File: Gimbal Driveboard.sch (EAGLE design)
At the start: 23 parts, among them J2 APP_2POS_CONFIG12V_HORIZ, U1 OKI-78SR-5/1.5-W36HC, U2 MAX232D, U3 MAX232D

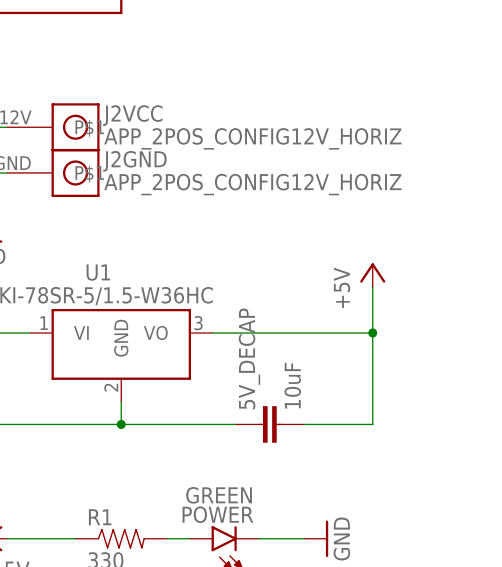
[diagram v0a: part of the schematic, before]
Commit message: Remade schematic to avoid physical interference with ethernet port
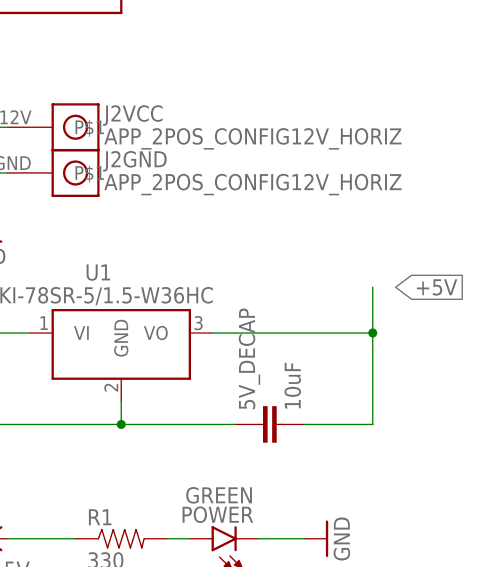
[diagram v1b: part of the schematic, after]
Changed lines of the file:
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@@
 <part name="GND7" library="supply1" deviceset="GND" device=""/>
 <part name="GND8" library="supply1" deviceset="GND" device=""/>
-<part name="P+14" library="supply1" deviceset="+5V" device=""/>
 <part name="GND20" library="supply1" deviceset="GND" device=""/>
 <part name="U1" library="MRDT-ICs" deviceset="OKI-78SR-*/1.5-W36?C" device="H" technology="5"/>
@@
 <instance part="GND7" gate="1" x="43.18" y="-5.08"/>
 <instance part="GND8" gate="1" x="91.44" y="-25.4"/>
-<instance part="P+14" gate="1" x="256.54" y="-43.18"/>
 <instance part="GND20" gate="1" x="213.36" y="-40.64"/>
 <instance part="U1" gate="G$1" x="226.06" y="-50.8"/>
@@
 </segment>
 <segment>
-<pinref part="P+14" gate="1" pin="+5V"/>
+<pinref part="R1" gate="G$1" pin="1"/>
+<pinref part="P+6" gate="1" pin="+5V"/>
+<wire x1="215.9" y1="-73.66" x2="223.52" y2="-73.66" width="0.1524" layer="91"/>
+</segment>
+<segment>
 <pinref part="5V_DECAP" gate="G$1" pin="2"/>
 <wire x1="248.92" y1="-60.96" x2="256.54" y2="-60.96" width="0.1524" layer="91"/>
@@
 <wire x1="238.76" y1="-50.8" x2="256.54" y2="-50.8" width="0.1524" layer="91"/>
 <junction x="256.54" y="-50.8"/>
-</segment>
-<segment>
-<pinref part="R1" gate="G$1" pin="1"/>
-<pinref part="P+6" gate="1" pin="+5V"/>
-<wire x1="215.9" y1="-73.66" x2="223.52" y2="-73.66" width="0.1524" layer="91"/>
+<label x="259.08" y="-45.72" size="1.778" layer="95" xref="yes"/>
 </segment>
 </net>

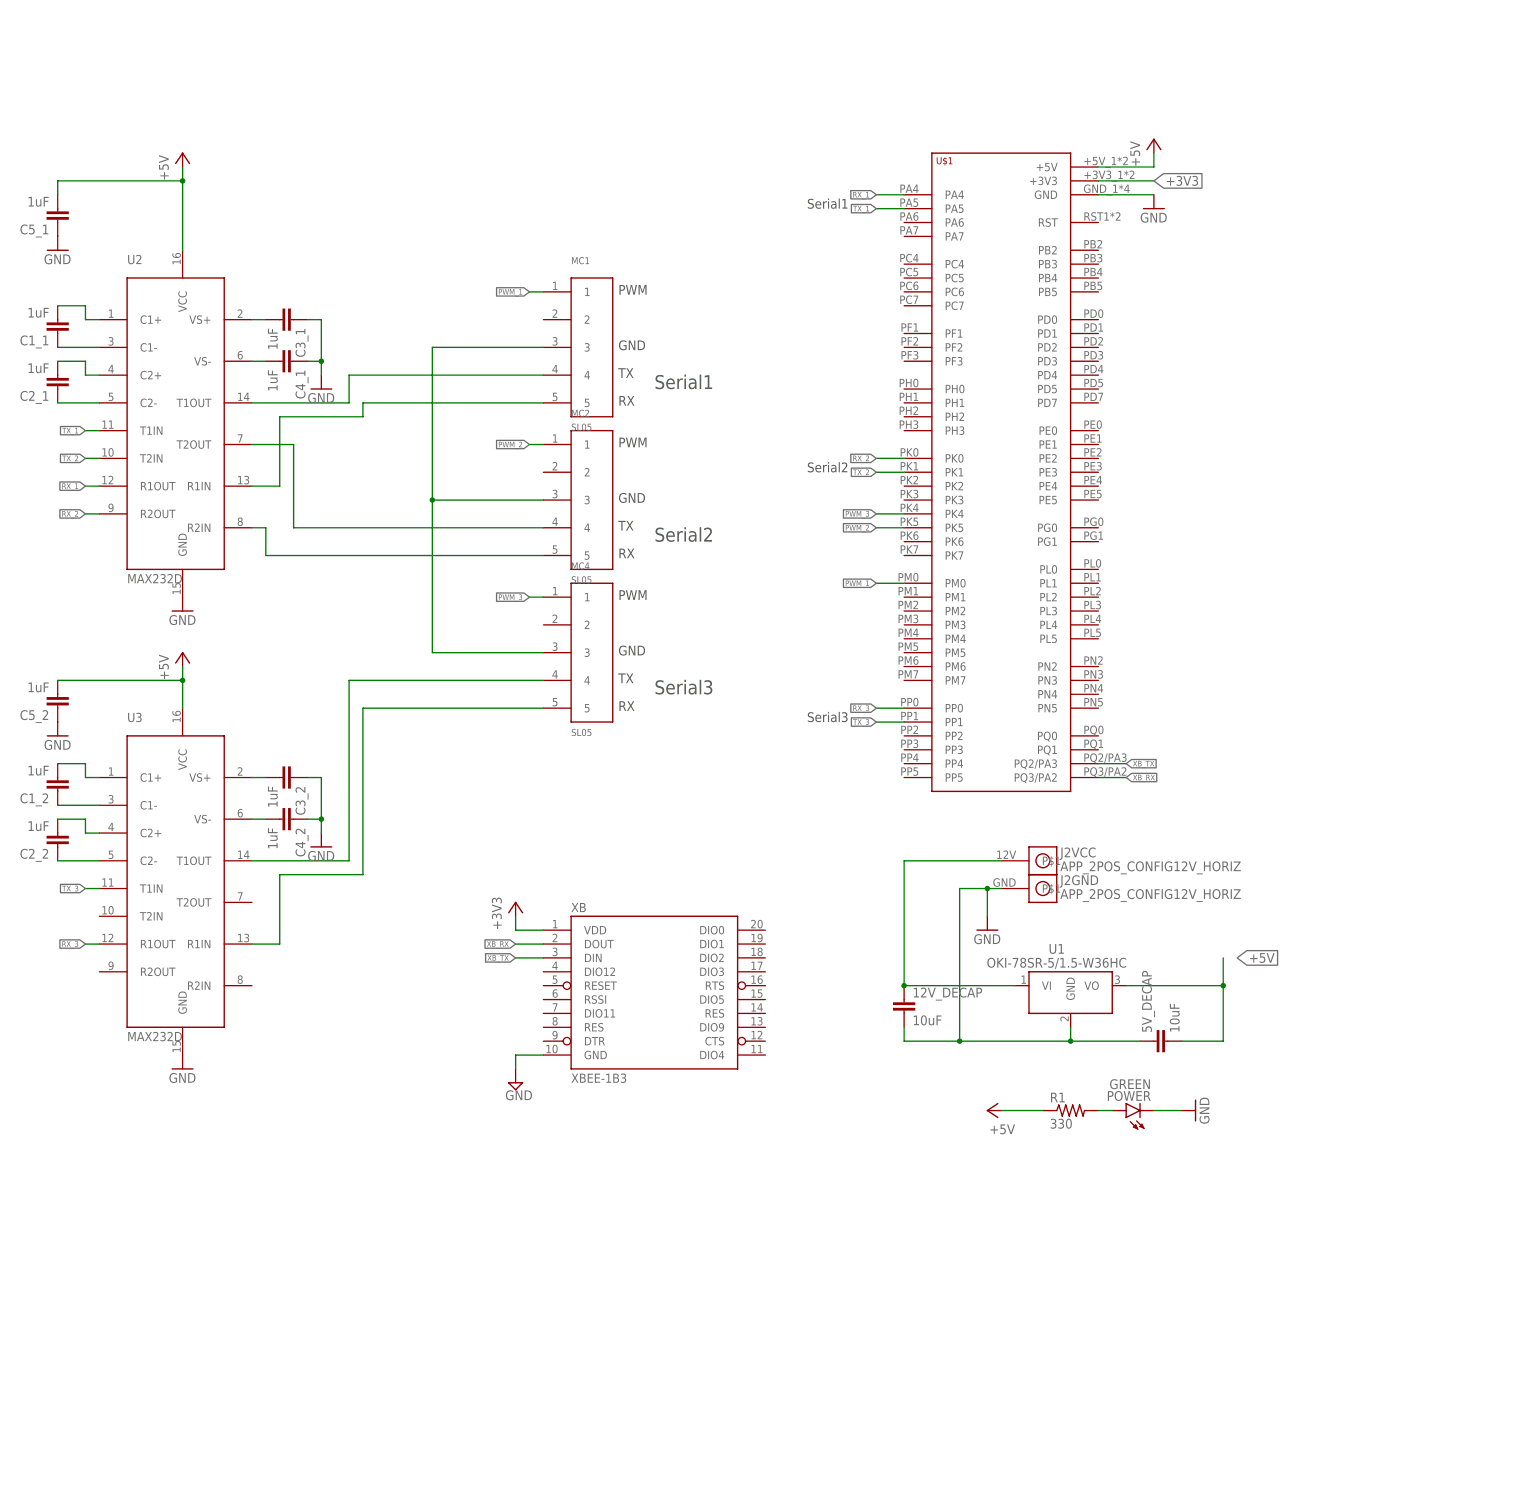
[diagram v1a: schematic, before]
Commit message: Updated schematic and board for final board review
added I2C Molex SL4
Added mounting tab and holes
cleaned up lines and traces
Added signature and board information
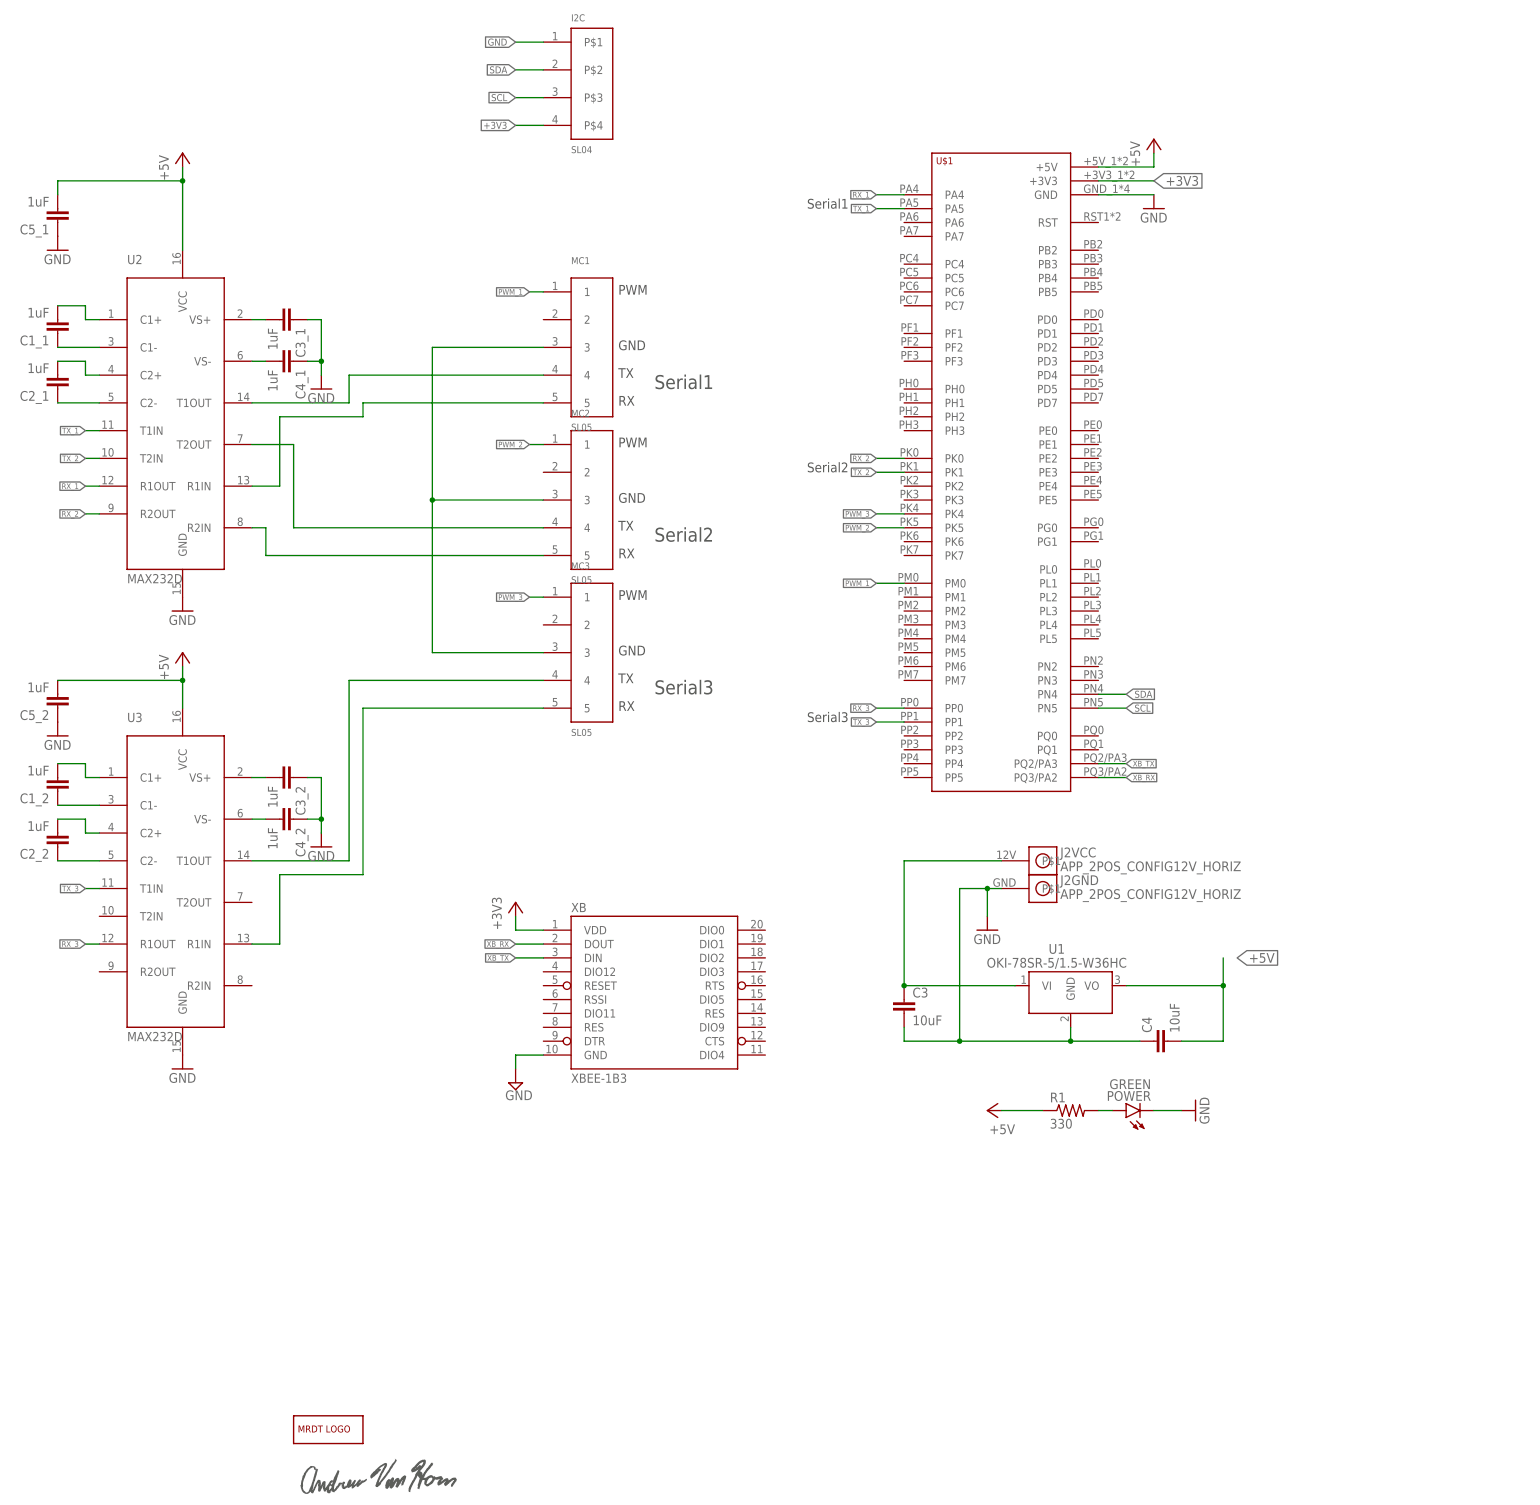
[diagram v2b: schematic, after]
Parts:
- added I2C: SL04, MRDT-Connectors:SL04
- added LOGO1: MRDT_LOGO, MRDT-Hardware:MRDT_LOGO
- added U$3: ANDREW_VAN_HORN_SIGNATURE, MRDT-Signatures:ANDREW_VAN_HORN_SIGNATURE
- renumbered 12V_DECAP to C3, 5V_DECAP to C4, MC4 to MC3
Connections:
- new net SCL: I2C.P$3, U$1.PN5
- new net SDA: I2C.P$2, U$1.PN4
- net +3V3: now also I2C.P$4
- net GND: now also I2C.P$1
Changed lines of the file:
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@@
 </variantdefs>
 <classes>
-<class number="0" name="default" width="0" drill="0">
+<class number="0" name="default" width="0.254" drill="0">
+<clearance class="0" value="0.254"/>
 </class>
 </classes>
@@
 <part name="MC1" library="MRDT-Connectors" deviceset="SL05" device="" value="SL05"/>
 <part name="MC2" library="MRDT-Connectors" deviceset="SL05" device="" value="SL05"/>
-<part name="MC4" library="MRDT-Connectors" deviceset="SL05" device="" value="SL05"/>
+<part name="MC3" library="MRDT-Connectors" deviceset="SL05" device="" value="SL05"/>
 <part name="P+3" library="supply1" deviceset="+5V" device=""/>
 <part name="GND3" library="supply1" deviceset="GND" device=""/>
@@
 <part name="U1" library="MRDT-ICs" deviceset="OKI-78SR-*/1.5-W36?C" device="H" technology="5"/>
 <part name="J2" library="MRDT-Connectors" deviceset="APP_2POS_CONFIG" device="12V_HORIZ"/>
-<part name="5V_DECAP" library="SparkFun-Capacitors" deviceset="CAP" device="0805" value="10uF"/>
-<part name="12V_DECAP" library="SparkFun-Capacitors" deviceset="CAP" device="0805" value="10uF"/>
+<part name="C4" library="SparkFun-Capacitors" deviceset="CAP" device="0805" value="10uF"/>
+<part name="C3" library="SparkFun-Capacitors" deviceset="CAP" device="0805" value="10uF"/>
 <part name="P+6" library="supply1" deviceset="+5V" device=""/>
 <part name="POWER" library="SparkFun-LED" deviceset="LED-GREEN" device="1206" value="GREEN"/>
@@
 <part name="+3V5" library="supply1" deviceset="+3V3" device=""/>
 <part name="SUPPLY6" library="supply2" deviceset="GND" device=""/>
+<part name="I2C" library="MRDT-Connectors" deviceset="SL04" device=""/>
+<part name="LOGO1" library="MRDT-Hardware" deviceset="MRDT_LOGO" device=""/>
+<part name="U$3" library="MRDT-Signatures" deviceset="ANDREW_VAN_HORN_SIGNATURE" device=""/>
 </parts>
 <sheets>
@@
 <instance part="MC1" gate="G$1" x="139.7" y="63.5"/>
 <instance part="MC2" gate="G$1" x="139.7" y="35.56"/>
-<instance part="MC4" gate="G$1" x="139.7" y="7.62"/>
+<instance part="MC3" gate="G$1" x="139.7" y="7.62"/>
 <instance part="P+3" gate="1" x="66.04" y="101.6"/>
 <instance part="GND3" gate="1" x="66.04" y="-66.04"/>
@@
 <instance part="J2" gate="GND" x="223.52" y="-33.02"/>
 <instance part="J2" gate="VCC" x="223.52" y="-27.94"/>
-<instance part="5V_DECAP" gate="G$1" x="246.38" y="-60.96" rot="R90"/>
-<instance part="12V_DECAP" gate="G$1" x="198.12" y="-55.88"/>
+<instance part="C4" gate="G$1" x="246.38" y="-60.96" rot="R90"/>
+<instance part="C3" gate="G$1" x="198.12" y="-55.88"/>
 <instance part="P+6" gate="1" x="213.36" y="-73.66" rot="R90"/>
 <instance part="POWER" gate="G$1" x="238.76" y="-73.66" rot="R90"/>
@@
 <instance part="+3V5" gate="G$1" x="127" y="-35.56"/>
 <instance part="SUPPLY6" gate="GND" x="127" y="-68.58"/>
+<instance part="I2C" gate="G$1" x="139.7" y="114.3"/>
+<instance part="LOGO1" gate="G$1" x="86.36" y="-134.62"/>
+<instance part="U$3" gate="G$1" x="86.36" y="-144.78"/>
 </instances>
 <busses>
@@
 <pinref part="MC2" gate="G$1" pin="3"/>
 <wire x1="132.08" y1="38.1" x2="111.76" y2="38.1" width="0.1524" layer="91"/>
-<pinref part="MC4" gate="G$1" pin="3"/>
+<pinref part="MC3" gate="G$1" pin="3"/>
 <wire x1="111.76" y1="38.1" x2="111.76" y2="10.16" width="0.1524" layer="91"/>
 <wire x1="111.76" y1="10.16" x2="132.08" y2="10.16" width="0.1524" layer="91"/>
@@
 <junction x="213.36" y="-33.02"/>
 <pinref part="J2" gate="GND" pin="P$1"/>
-<pinref part="12V_DECAP" gate="G$1" pin="2"/>
+<pinref part="C3" gate="G$1" pin="2"/>
 <wire x1="198.12" y1="-58.42" x2="198.12" y2="-60.96" width="0.1524" layer="91"/>
 <wire x1="198.12" y1="-60.96" x2="208.28" y2="-60.96" width="0.1524" layer="91"/>
 <junction x="208.28" y="-60.96"/>
-<pinref part="5V_DECAP" gate="G$1" pin="1"/>
+<pinref part="C4" gate="G$1" pin="1"/>
 <wire x1="241.3" y1="-60.96" x2="228.6" y2="-60.96" width="0.1524" layer="91"/>
 <junction x="228.6" y="-60.96"/>
@@
 <wire x1="127" y1="-63.5" x2="127" y2="-66.04" width="0.1524" layer="91"/>
 <pinref part="SUPPLY6" gate="GND" pin="GND"/>
+</segment>
+<segment>
+<pinref part="I2C" gate="G$1" pin="P$1"/>
+<wire x1="132.08" y1="121.92" x2="127" y2="121.92" width="0.1524" layer="91"/>
+<label x="127" y="121.92" size="1.27" layer="95" rot="R180" xref="yes"/>
 </segment>
 </net>
@@
 </segment>
 <segment>
-<pinref part="5V_DECAP" gate="G$1" pin="2"/>
+<pinref part="C4" gate="G$1" pin="2"/>
 <wire x1="248.92" y1="-60.96" x2="256.54" y2="-60.96" width="0.1524" layer="91"/>
 <wire x1="256.54" y1="-60.96" x2="256.54" y2="-50.8" width="0.1524" layer="91"/>
@@
 </segment>
 <segment>
-<pinref part="MC4" gate="G$1" pin="1"/>
+<pinref part="MC3" gate="G$1" pin="1"/>
 <wire x1="132.08" y1="20.32" x2="129.54" y2="20.32" width="0.1524" layer="91"/>
 <label x="129.54" y="20.32" size="1.016" layer="95" rot="R180" xref="yes"/>
@@
 <pinref part="U3" gate="G$1" pin="T1OUT"/>
 <wire x1="78.74" y1="-27.94" x2="96.52" y2="-27.94" width="0.1524" layer="91"/>
-<pinref part="MC4" gate="G$1" pin="4"/>
+<pinref part="MC3" gate="G$1" pin="4"/>
 <wire x1="96.52" y1="-27.94" x2="96.52" y2="5.08" width="0.1524" layer="91"/>
 <wire x1="96.52" y1="5.08" x2="132.08" y2="5.08" width="0.1524" layer="91"/>
@@
 <wire x1="83.82" y1="-43.18" x2="83.82" y2="-30.48" width="0.1524" layer="91"/>
 <wire x1="83.82" y1="-30.48" x2="99.06" y2="-30.48" width="0.1524" layer="91"/>
-<pinref part="MC4" gate="G$1" pin="5"/>
+<pinref part="MC3" gate="G$1" pin="5"/>
 <wire x1="132.08" y1="0" x2="99.06" y2="0" width="0.1524" layer="91"/>
 <wire x1="99.06" y1="0" x2="99.06" y2="-30.48" width="0.1524" layer="91"/>
@@
 <wire x1="198.12" y1="-27.94" x2="198.12" y2="-50.8" width="0.1524" layer="91"/>
 <pinref part="J2" gate="VCC" pin="P$1"/>
-<pinref part="12V_DECAP" gate="G$1" pin="1"/>
+<pinref part="C3" gate="G$1" pin="1"/>
 <junction x="198.12" y="-50.8"/>
 <pinref part="U1" gate="G$1" pin="VI"/>
@@
 <label x="243.84" y="96.52" size="1.778" layer="95" xref="yes"/>
 </segment>
+<segment>
+<pinref part="I2C" gate="G$1" pin="P$4"/>
+<wire x1="132.08" y1="106.68" x2="127" y2="106.68" width="0.1524" layer="91"/>
+<label x="127" y="106.68" size="1.27" layer="95" rot="R180" xref="yes"/>
+</segment>
 </net>
 <net name="XB_RX" class="0">
@@
 </segment>
 </net>
+<net name="SDA" class="0">
+<segment>
+<pinref part="I2C" gate="G$1" pin="P$2"/>
+<wire x1="132.08" y1="116.84" x2="127" y2="116.84" width="0.1524" layer="91"/>
+<label x="127" y="116.84" size="1.27" layer="95" rot="R180" xref="yes"/>
+</segment>
+<segment>
+<pinref part="U$1" gate="G$1" pin="PN4"/>
+<wire x1="233.68" y1="2.54" x2="238.76" y2="2.54" width="0.1524" layer="91"/>
+<label x="238.76" y="2.54" size="1.27" layer="95" xref="yes"/>
+</segment>
+</net>
+<net name="SCL" class="0">
+<segment>
+<pinref part="I2C" gate="G$1" pin="P$3"/>
+<wire x1="132.08" y1="111.76" x2="127" y2="111.76" width="0.1524" layer="91"/>
+<label x="127" y="111.76" size="1.27" layer="95" rot="R180" xref="yes"/>
+</segment>
+<segment>
+<pinref part="U$1" gate="G$1" pin="PN5"/>
+<wire x1="233.68" y1="0" x2="238.76" y2="0" width="0.1524" layer="91"/>
+<label x="238.76" y="0" size="1.27" layer="95" xref="yes"/>
+</segment>
+</net>
